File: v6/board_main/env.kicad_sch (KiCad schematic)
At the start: 0 parts

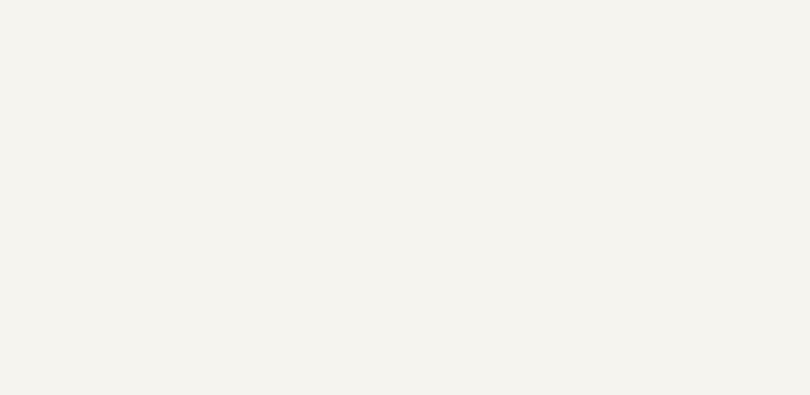
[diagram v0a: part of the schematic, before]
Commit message: Remove old artefacts and add mcu schematic to ENV6 main
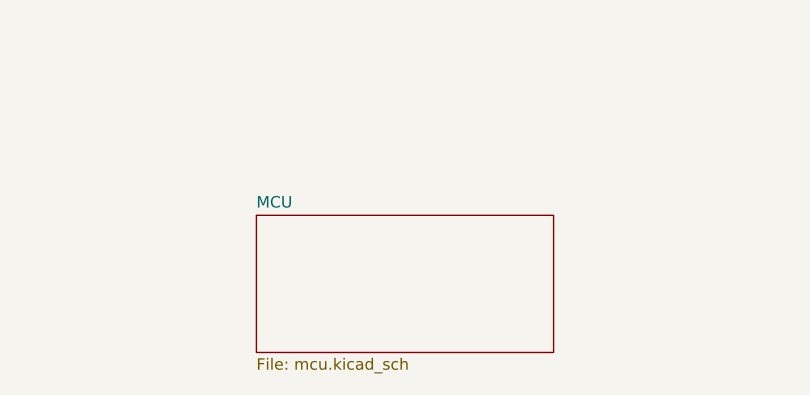
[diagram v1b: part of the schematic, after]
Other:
- added sheet MCU (mcu.kicad_sch)
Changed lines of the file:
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@@
+	)
+	(sheet
+		(at 119.38 76.2)
+		(size 33.02 15.24)
+		(exclude_from_sim no)
+		(in_bom yes)
+		(on_board yes)
+		(dnp no)
+		(fields_autoplaced yes)
+		(stroke
+			(width 0.1524)
+			(type solid)
+		)
+		(fill
+			(color 0 0 0 0.0000)
+		)
+		(property "Sheetname" "MCU"
+			(at 119.38 75.4884 0)
+			(effects
+				(font
+					(size 1.27 1.27)
+				)
+				(justify left bottom)
+			)
+		)
+		(property "Sheetfile" "mcu.kicad_sch"
+			(at 119.38 92.0246 0)
+			(effects
+				(font
+					(size 1.27 1.27)
+				)
+				(justify left top)
+			)
+		)
+		(instances
+			(project "env"
+				(path "/4c59d168-fd3a-43d1-bf01-995dc1715e36"
+					(page "8")
+				)
+			)
+		)
 	)
 	(sheet

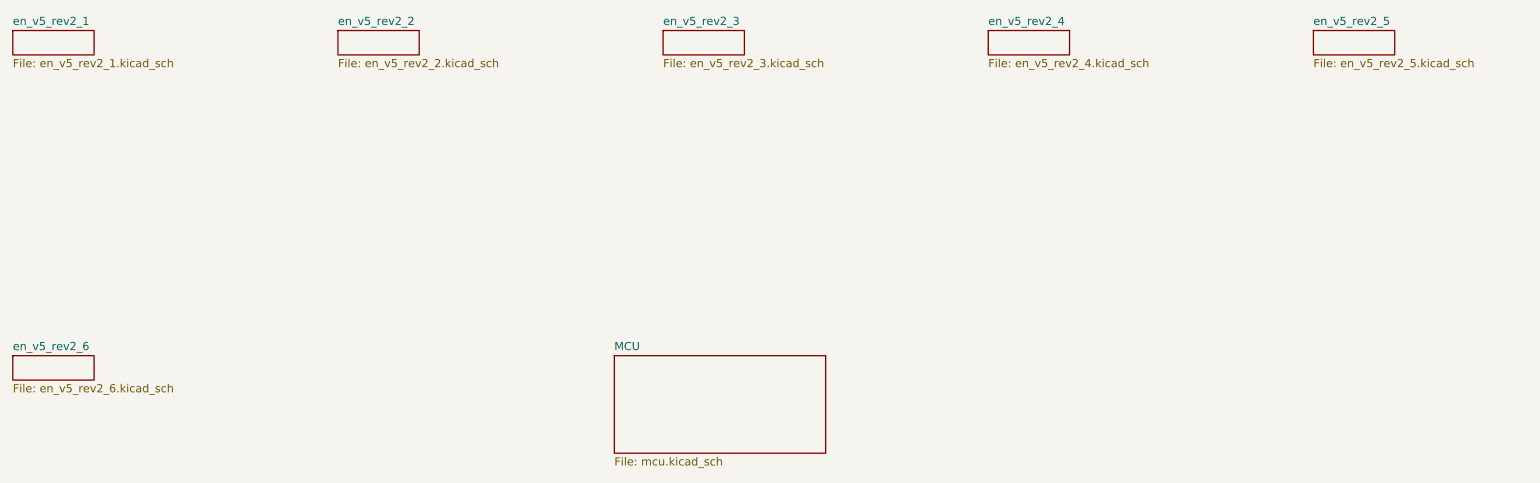
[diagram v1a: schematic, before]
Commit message: Rephrasing ENV5 design
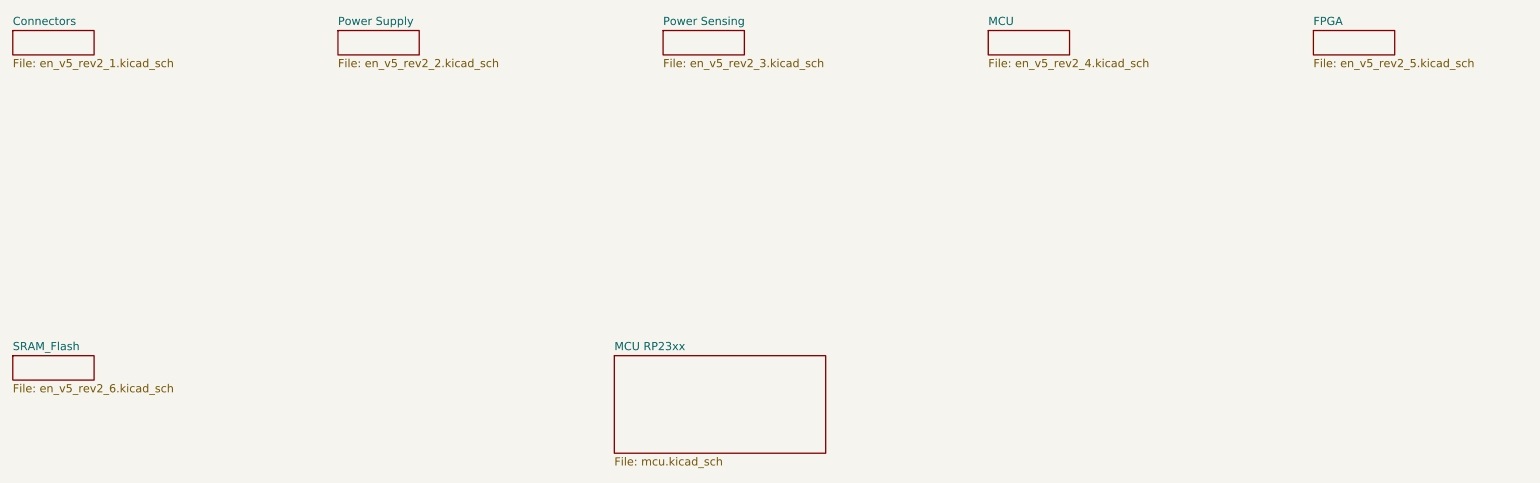
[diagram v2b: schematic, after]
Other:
- sheet en_v5_rev2_1 renamed Connectors
- sheet en_v5_rev2_2 renamed Power Supply
- sheet en_v5_rev2_3 renamed Power Sensing
- sheet en_v5_rev2_5 renamed FPGA
- sheet en_v5_rev2_6 renamed SRAM_Flash
- removed sheet en_v5_rev2_4
- added sheet MCU RP23xx (mcu.kicad_sch)
- sheet MCU: file mcu.kicad_sch -> en_v5_rev2_4.kicad_sch
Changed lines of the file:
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@@
 			(color 0 0 0 0.0000)
 		)
-		(property "Sheetname" "en_v5_rev2_5"
+		(property "Sheetname" "FPGA"
 			(at 228.6 24.6884 0)
 			(effects
@@
 			(color 0 0 0 0.0000)
 		)
-		(property "Sheetname" "en_v5_rev2_2"
+		(property "Sheetname" "Power Supply"
 			(at 76.2 24.6884 0)
 			(effects
@@
 			(color 0 0 0 0.0000)
 		)
-		(property "Sheetname" "en_v5_rev2_3"
+		(property "Sheetname" "Power Sensing"
 			(at 127 24.6884 0)
 			(effects
@@
 			(color 0 0 0 0.0000)
 		)
-		(property "Sheetname" "en_v5_rev2_4"
+		(property "Sheetname" "MCU"
 			(at 177.8 24.6884 0)
 			(effects
@@
 			(color 0 0 0 0.0000)
 		)
-		(property "Sheetname" "en_v5_rev2_1"
+		(property "Sheetname" "Connectors"
 			(at 25.4 24.6884 0)
 			(effects
@@
 		(at 119.38 76.2)
 		(size 33.02 15.24)
-		(exclude_from_sim no)
-		(in_bom yes)
-		(on_board yes)
-		(dnp no)
+		(exclude_from_sim yes)
+		(in_bom no)
+		(on_board no)
+		(dnp yes)
 		(fields_autoplaced yes)
 		(stroke
@@
 			(color 0 0 0 0.0000)
 		)
-		(property "Sheetname" "MCU"
+		(property "Sheetname" "MCU RP23xx"
 			(at 119.38 75.4884 0)
 			(effects
@@
 			(project "env"
 				(path "/4c59d168-fd3a-43d1-bf01-995dc1715e36"
-					(page "8")
+					(page "7")
 				)
 			)
@@
 			(color 0 0 0 0.0000)
 		)
-		(property "Sheetname" "en_v5_rev2_6"
+		(property "Sheetname" "SRAM_Flash"
 			(at 25.4 75.4884 0)
 			(effects

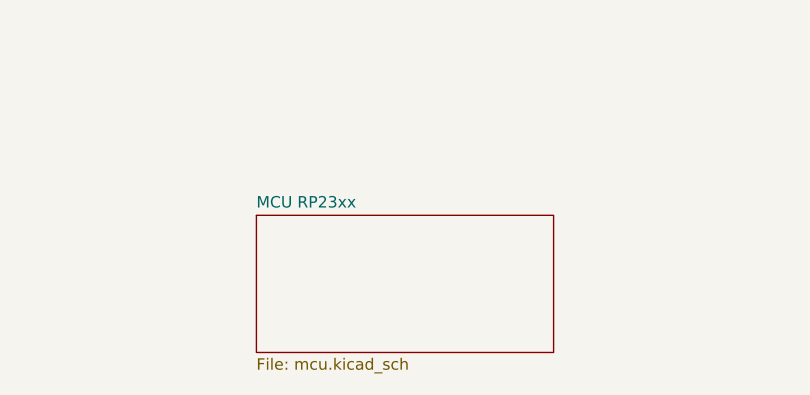
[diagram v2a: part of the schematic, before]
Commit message: Add design of ENV6 mini
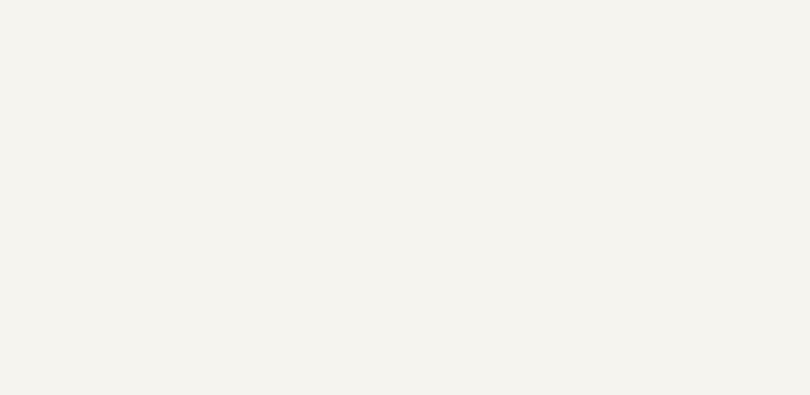
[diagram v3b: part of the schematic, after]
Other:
- removed sheet MCU RP23xx
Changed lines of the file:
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@@
-	)
-	(sheet
-		(at 119.38 76.2)
-		(size 33.02 15.24)
-		(exclude_from_sim yes)
-		(in_bom no)
-		(on_board no)
-		(dnp yes)
-		(fields_autoplaced yes)
-		(stroke
-			(width 0.1524)
-			(type solid)
-		)
-		(fill
-			(color 0 0 0 0.0000)
-		)
-		(property "Sheetname" "MCU RP23xx"
-			(at 119.38 75.4884 0)
-			(effects
-				(font
-					(size 1.27 1.27)
-				)
-				(justify left bottom)
-			)
-		)
-		(property "Sheetfile" "mcu.kicad_sch"
-			(at 119.38 92.0246 0)
-			(effects
-				(font
-					(size 1.27 1.27)
-				)
-				(justify left top)
-			)
-		)
-		(instances
-			(project "env"
-				(path "/4c59d168-fd3a-43d1-bf01-995dc1715e36"
-					(page "7")
-				)
-			)
-		)
 	)
 	(sheet
